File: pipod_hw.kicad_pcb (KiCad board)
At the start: 4 copper layers, 55.5 x 96.8 mm, 172 parts, among them J1 Conn_01x03_Male, J2 USB_C_Receptacle_USB2.0, J3 SFV8R-2STE1HLF, J4 SFV14R-2STE1HLF, J5 2-1734839-5, J6 S7051-42R, J7 S7051-42R, Q1 DMG9926UDM, Q2 NTK3139PT1G, Q3 BSS138, SW1 SW_Push, SW2 SW_Push, U1 MAX17048G+T10, U10 TPS22965TDSGRQ1, U11 TPS22965TDSGRQ1, U12 TPS22965TDSGRQ1, U13 PCM5102APWR, U14 PAM8908JER, U15 MCP23008-E/ML, U2 MAX8903AETI+T, U3 BQ29728DSER, U4 XC6210B332MR, U5 W25Q128JVS, U6 RP2040, U7 NLAS7242MUTBG, U8 RS2299XTQC16, U9 TPS22965TDSGRQ1, Y1 12MHz 20pF

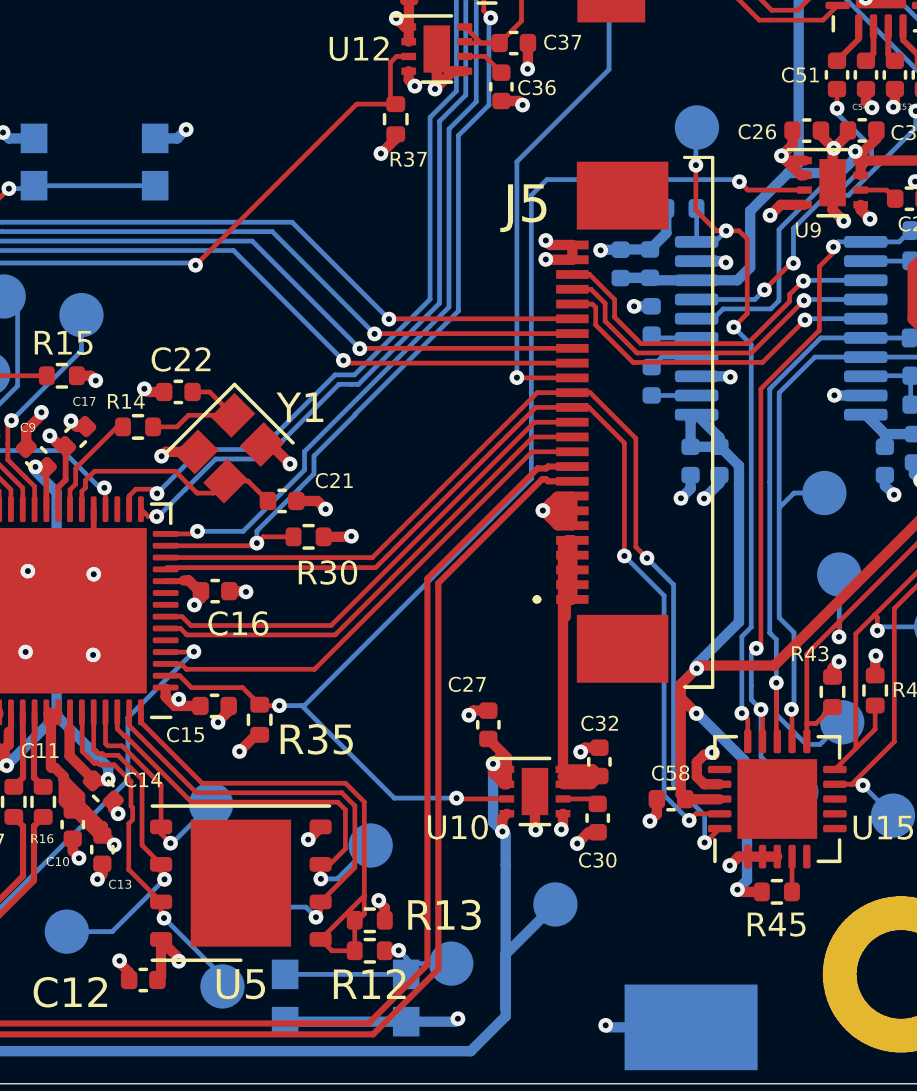
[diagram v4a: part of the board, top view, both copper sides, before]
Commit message: schematic: add resistors to allow latching pi power
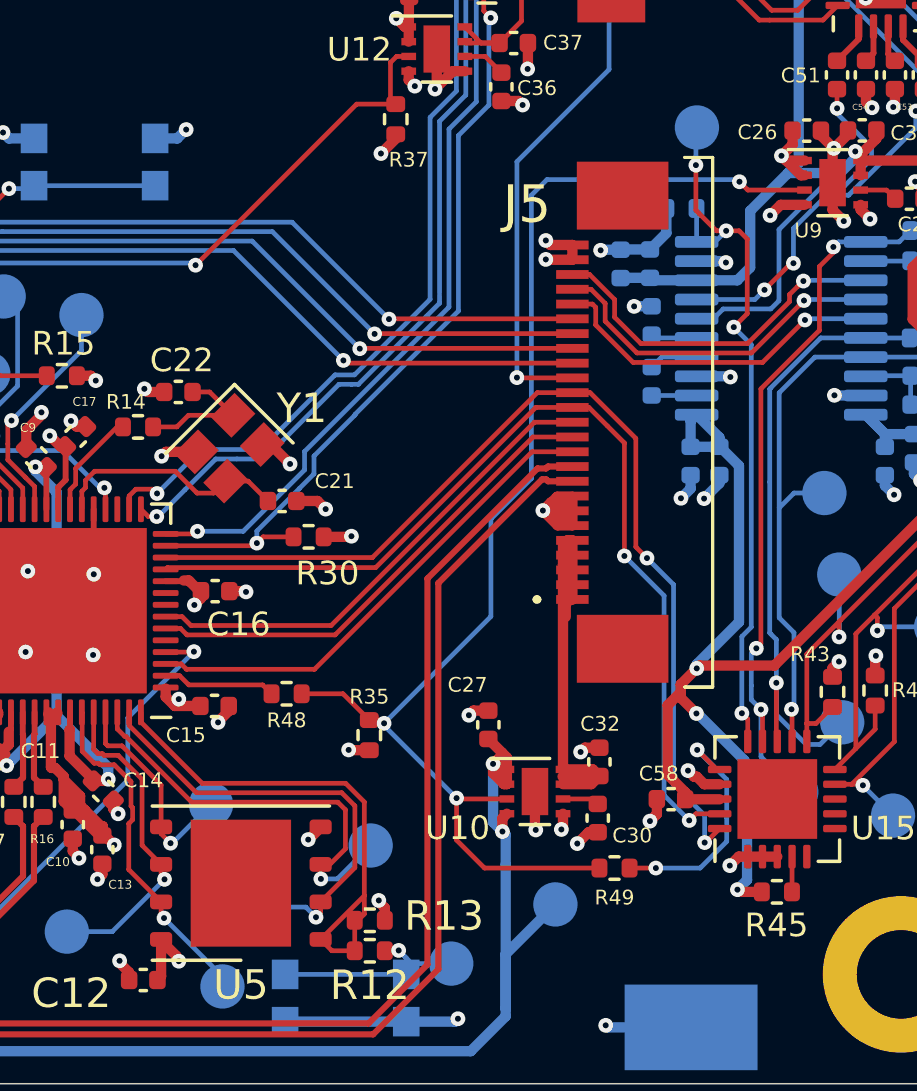
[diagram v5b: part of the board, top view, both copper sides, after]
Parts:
- added R48: 1k, Resistor_SMD:R_0402_1005Metric, F.Cu at (29.6, 35.3)
- added R49: 1k, Resistor_SMD:R_0402_1005Metric, F.Cu at (40.7, 41.2)
- moved R35 3.75 mm to (32.4, 36.7)
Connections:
- R35 pad 2: PI_VCC_EN -> PI_LOAD_SWITCH_EN
- U10 pad 3: PI_VCC_EN -> PI_LOAD_SWITCH_EN
- U15 pad 16: unconnected-(U15-Pad16) -> /Pi/PI_VCC_LATCH
- U6 pad 2: PI_VCC_EN -> /SMC/PI_VCC_EN
- U9 pad 3: PI_VCC_EN -> PI_LOAD_SWITCH_EN
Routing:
- net PI_LOAD_SWITCH_EN: track 0.00 -> 44.7 mm, vias 0 -> 3
- net PI_VCC_EN: track 43.4 -> 0.00 mm, vias 3 -> 0
- net /Pi/PI_VCC_LATCH: track 0.00 -> 8.21 mm, vias 0 -> 2
- net /SMC/PI_VCC_EN: track 0.00 -> 3.84 mm
- net GND: track 143.3 -> 142.2 mm

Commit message: compute: finish layout and routing
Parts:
- added D4: GRN, LED_SMD:LED_0402_1005Metric, B.Cu at (27.8, 33.6)
- added R50: 470R, Resistor_SMD:R_0402_1005Metric, B.Cu at (29.8, 33.6)
- added TP34: TestPoint, TestPoint:TestPoint_Pad_D1.5mm, B.Cu at (32.2, 33.7)
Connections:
- J5 pad 12: SMC_RX_PI_TX -> SMC_TX_PI_RX
- J5 pad 13: SMC_TX_PI_RX -> SMC_RX_PI_TX
- U6 pad 5: unconnected-(U6-Pad5) -> SMC_LED
- U6 pad 6: SMC_RX_PI_TX -> SMC_TX_PI_RX
- U6 pad 7: SMC_TX_PI_RX -> SMC_RX_PI_TX
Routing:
- net SMC_LED: track 0.00 -> 8.13 mm, vias 0 -> 1
- net Net-(D4-Pad1): track 0.00 -> 1.00 mm
- net GND: track 142.2 -> 142.7 mm, vias 111 -> 112

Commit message: ci: prepare files for CI
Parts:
- L1: footprint Inductor_SMD:L_Vishay_IFSC-1515AH_4x4x1.8mm -> Gigahawk:L_Vishay_IFSC-1515AH_4x4x1.8mm
- Q2: footprint Package_TO_SOT_SMD:SOT-723 -> Gigahawk:SOT-723
- U1: footprint Package_DFN_QFN:DFN-8-1EP_2x2mm_P0.5mm_EP0.6x1.2mm -> Gigahawk:DFN-8-1EP_2x2mm_P0.5mm_EP0.6x1.2mm
- U14, U8: footprint Package_DFN_QFN:QFN-16-1EP_3x3mm_P0.5mm_EP1.7x1.7mm -> Gigahawk:QFN-16-1EP_3x3mm_P0.5mm_EP1.7x1.7mm
- U15: footprint Package_DFN_QFN:QFN-20-1EP_4x4mm_P0.5mm_EP2.7x2.7mm -> Gigahawk:QFN-20-1EP_4x4mm_P0.5mm_EP2.7x2.7mm
- U2: footprint Package_DFN_QFN:QFN-28-1EP_4x4mm_P0.4mm_EP2.6x2.6mm -> Gigahawk:QFN-28-1EP_4x4mm_P0.4mm_EP2.6x2.6mm
- U5: footprint Package_SON:WSON-8-1EP_6x5mm_P1.27mm_EP3.4x4.3mm -> Gigahawk:WSON-8-1EP_6x5mm_P1.27mm_EP3.4x4.3mm
- Y1: footprint Crystal:Crystal_SMD_2520-4Pin_2.5x2.0mm -> Gigahawk:Crystal_SMD_2520-4Pin_2.5x2.0mm
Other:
- board text added: "Layers: 4 PCB thickness: 0.8mm Material: FR-4 TG 150-160 Outer Copper: 1oz Inner Copper: 1oz"
- board text added: "PCBWAYPCBWAY"
- board text added: "piPod SMC Board ${TAG} (${REVISION})"
- board text removed: "Connect LCK_COM to DGND to unlock controls"
- board text removed: "JLCJLCJLCJLC"
- board text removed: "Layers: 4 PCB thickness: 0.8mm Impedance: Yes (JLC7628)"

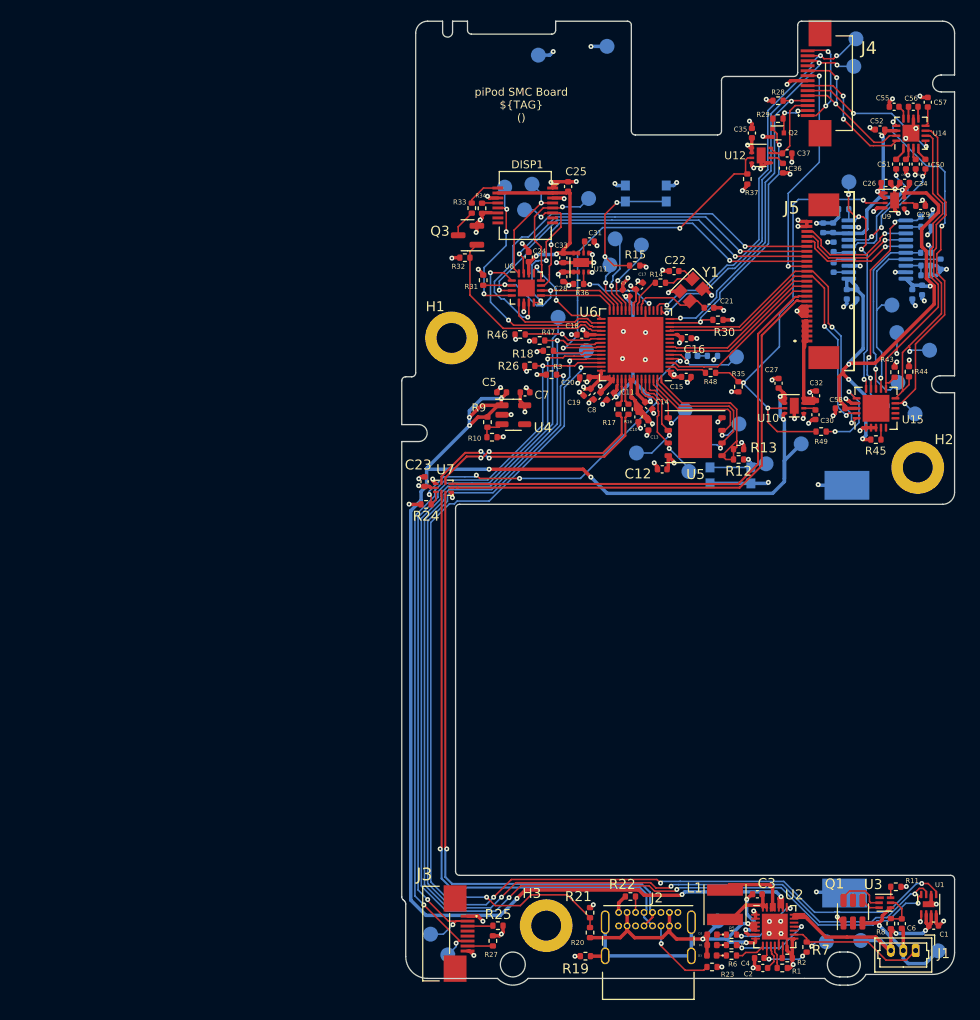
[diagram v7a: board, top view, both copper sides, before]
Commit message: smc: update constraints to match cheaper pcbway tier
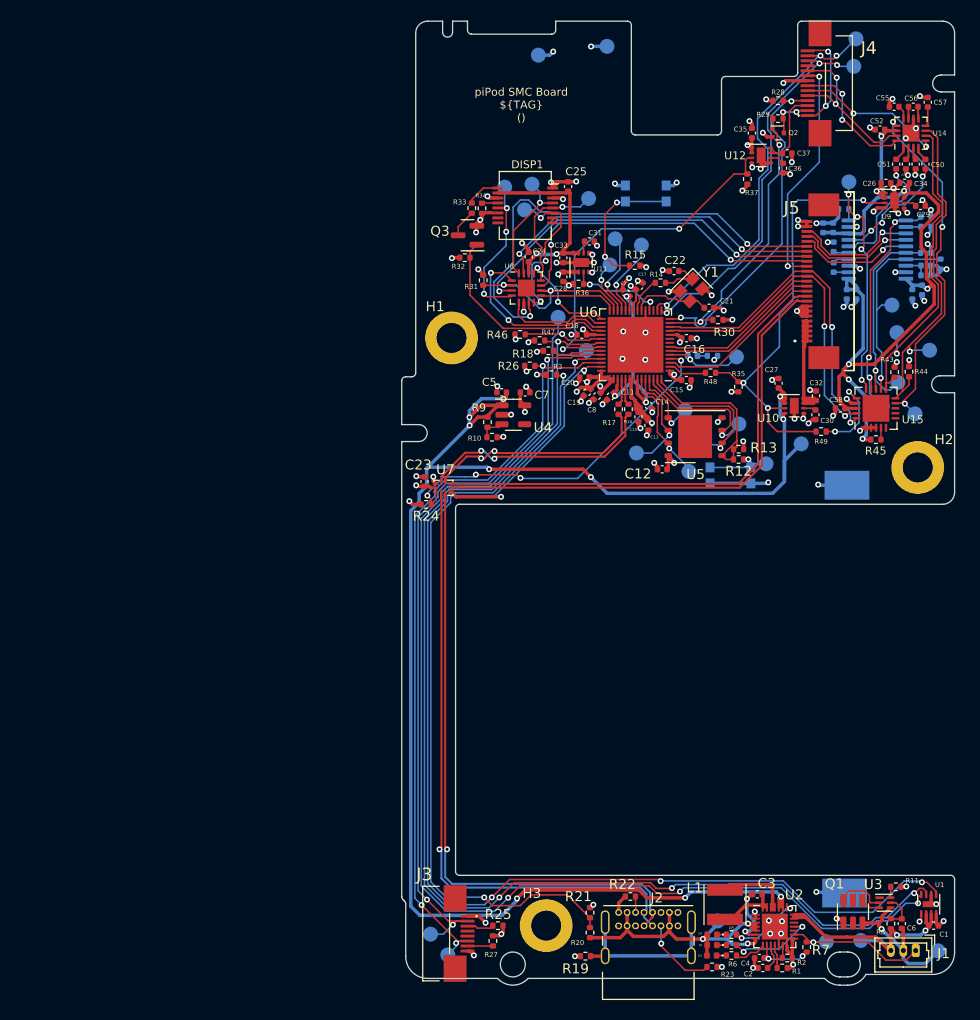
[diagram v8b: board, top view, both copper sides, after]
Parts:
- moved C15 0.32 mm to (27.2, 36.0)
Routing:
- net GND: track 142.7 -> 148.0 mm
- net PI_DISP_RST: track 43.5 -> 47.5 mm
- net HP_LCK: track 31.0 -> 34.7 mm
- net +3V3: track 57.3 -> 60.2 mm
- net VCC: track 161.7 -> 162.6 mm
- net PI_AMP_EN: track 36.5 -> 35.6 mm
- net SMC_RMT_RX: track 40.5 -> 41.3 mm
- net +1V1: track 21.0 -> 20.3 mm
- net DISP_INPUT_SEL: track 18.9 -> 19.5 mm
- net ~{CHRG_FLT}: track 8.28 -> 8.78 mm
